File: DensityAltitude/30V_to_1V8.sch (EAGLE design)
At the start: 14 parts, among them U1 V_REG_LD1086V

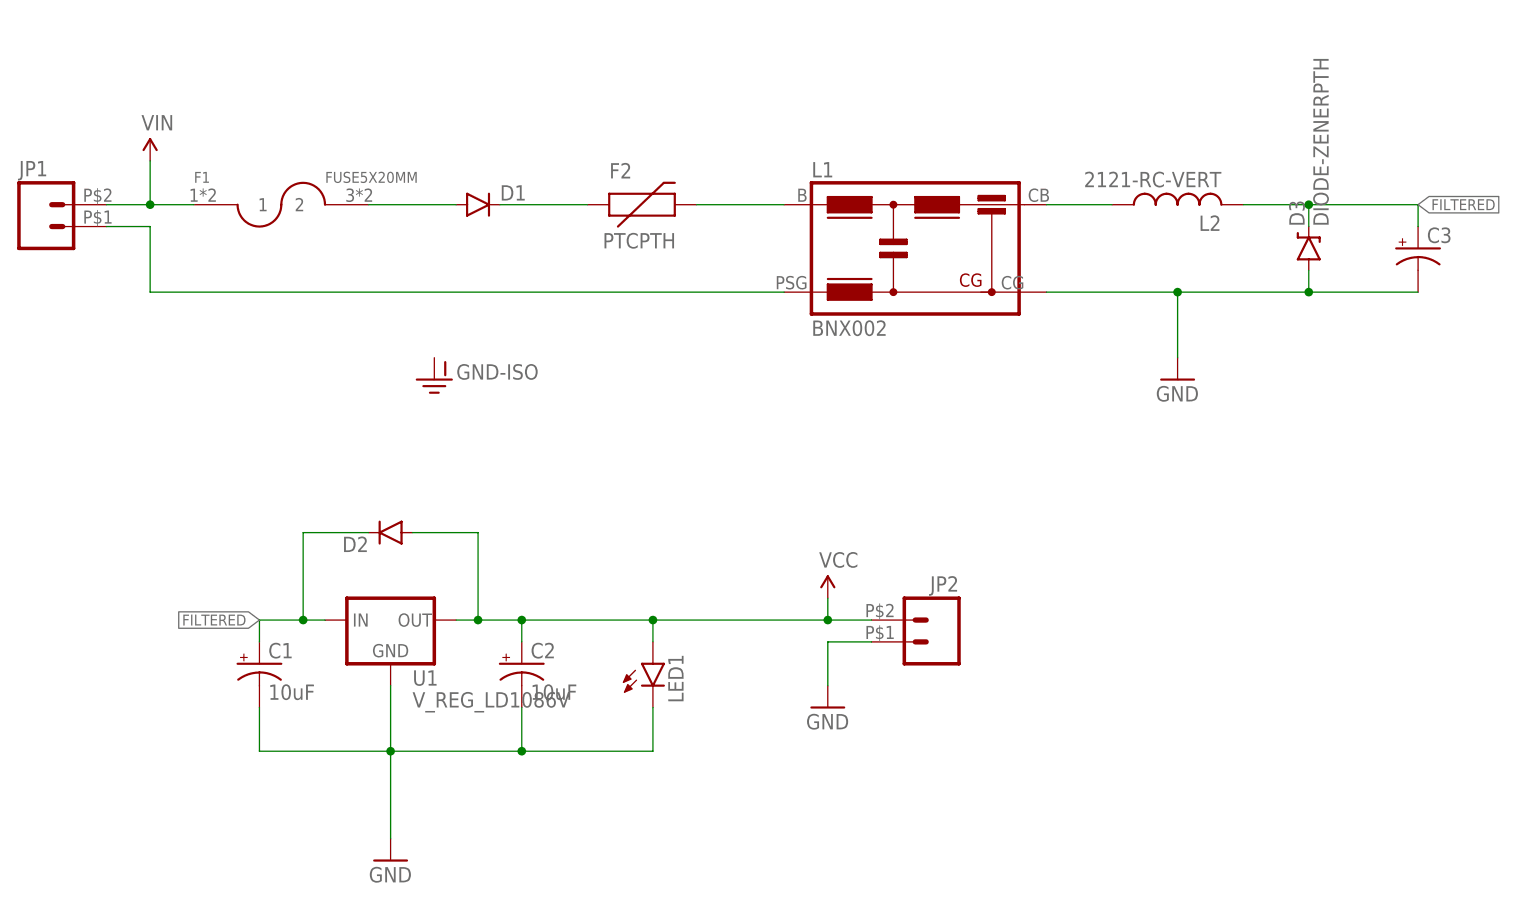
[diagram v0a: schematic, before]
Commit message: Moved 1V8 voltage regulators from DensityAltitude.lbr to 1V8.lbr More layout work for various high input voltage regulators A bit more work on LowduinoPTH_v2
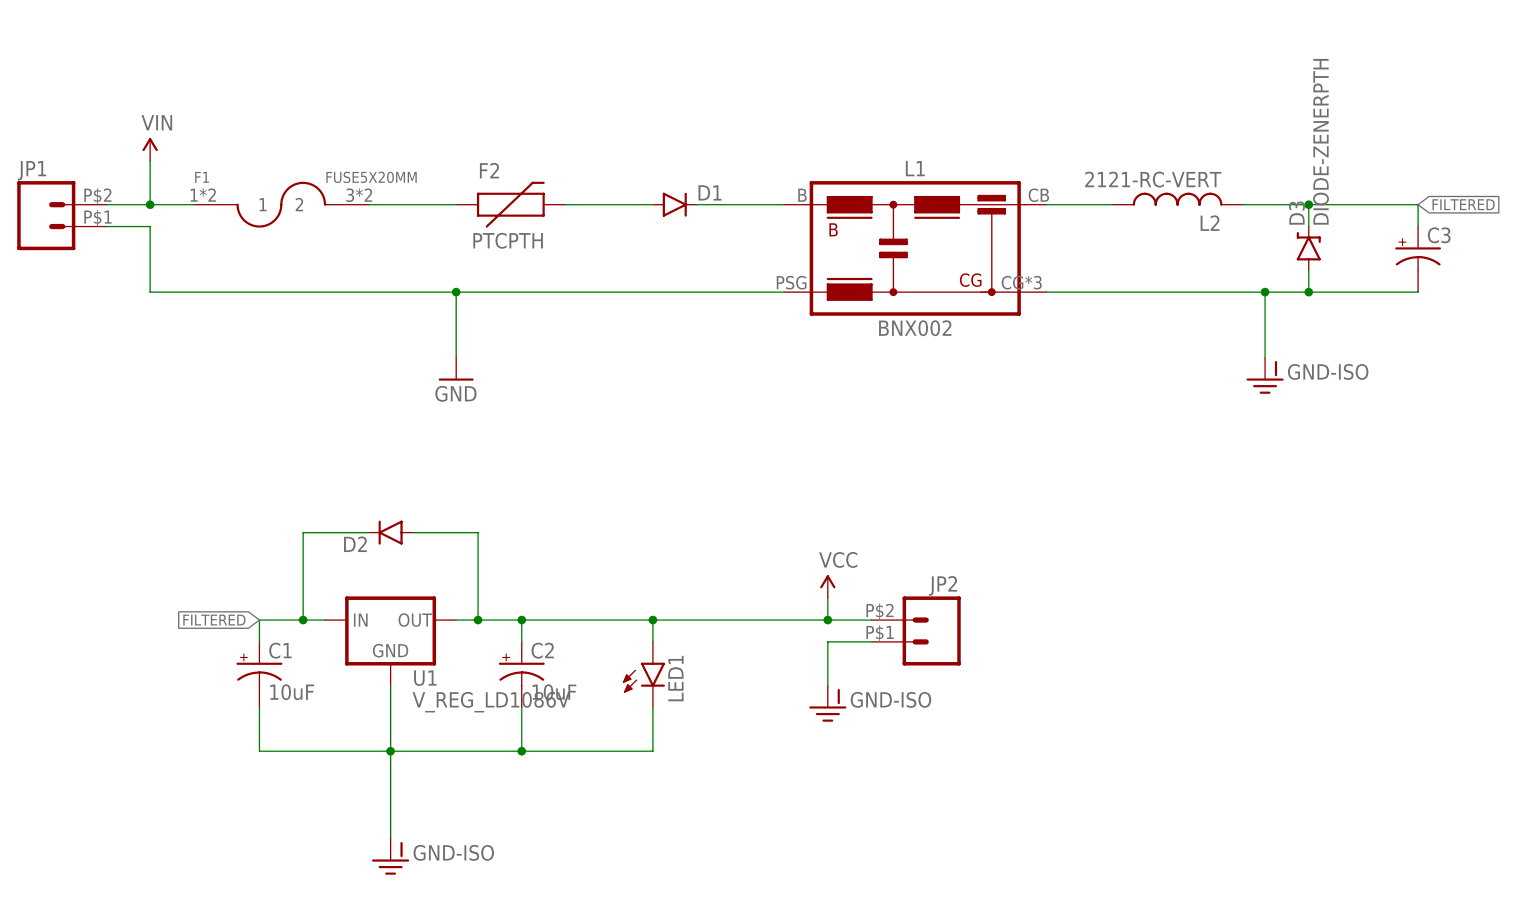
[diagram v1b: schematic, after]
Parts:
- C1, C2: device rcl:CPOL-USE2-5 -> 1V8:10UF-50V-10%(PTH)
- L1: device inductors:BNX002 -> 1V8:BNX002
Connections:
- removed net N$3: JP1.1, L1.PSG
- new net GND-ISO: C1.-, C2.-, C3.-, D3.A, JP2.1, L1.CG, LED1.C, U1.GND
- net DIODE1: now also L1.B; no longer F2.1
- net FUSE1: now also F2.1; no longer D1.A
- net FUSE2: now also D1.A; no longer L1.B
- net GND: now also JP1.1, L1.PSG; no longer C1.-, C2.-, C3.-, D3.A, JP2.1, L1.CG, LED1.C, U1.GND
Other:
- moved on the sheet: D1, F2
